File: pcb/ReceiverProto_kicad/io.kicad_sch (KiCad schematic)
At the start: 4 parts, among them J1 Conn_01x09, J2 Conn_01x03, J3 Conn_01x03, J4 Conn_01x06

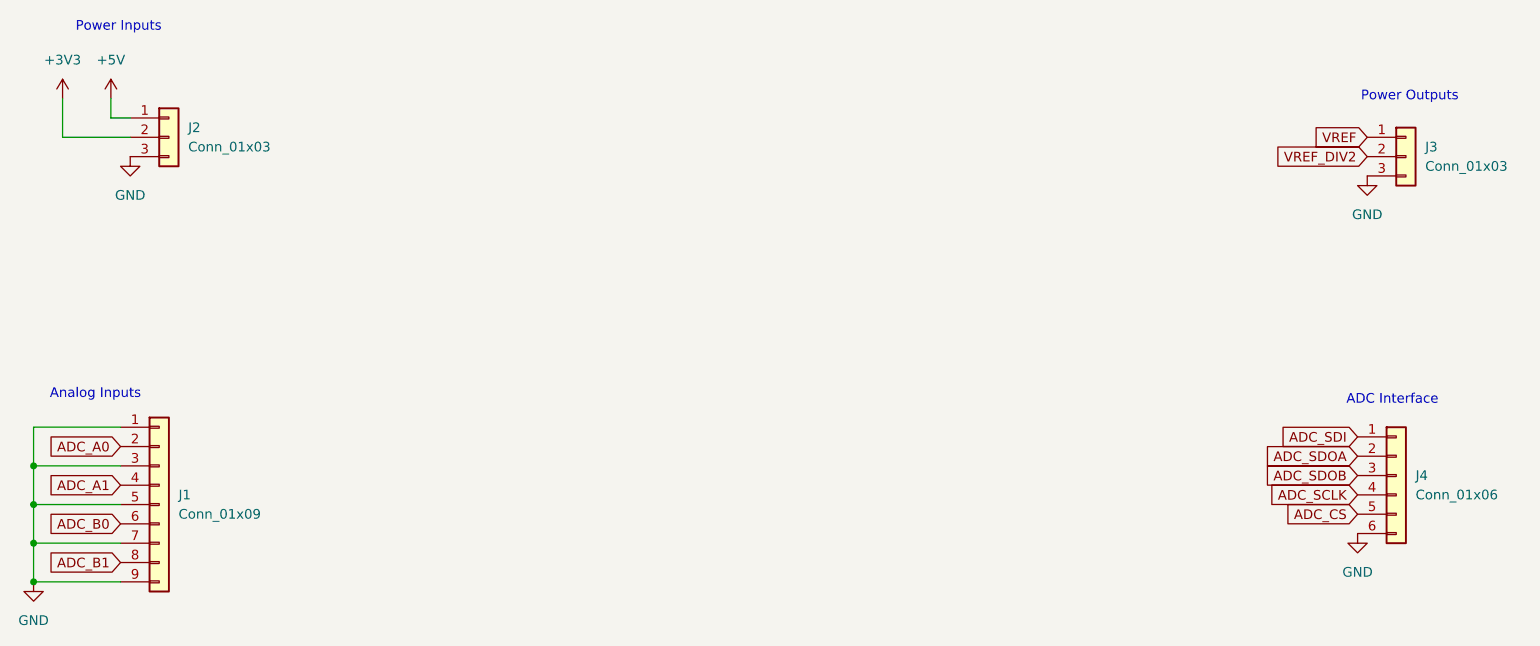
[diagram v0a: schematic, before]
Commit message: fixed kicad project, all footprints linked and no errors on board
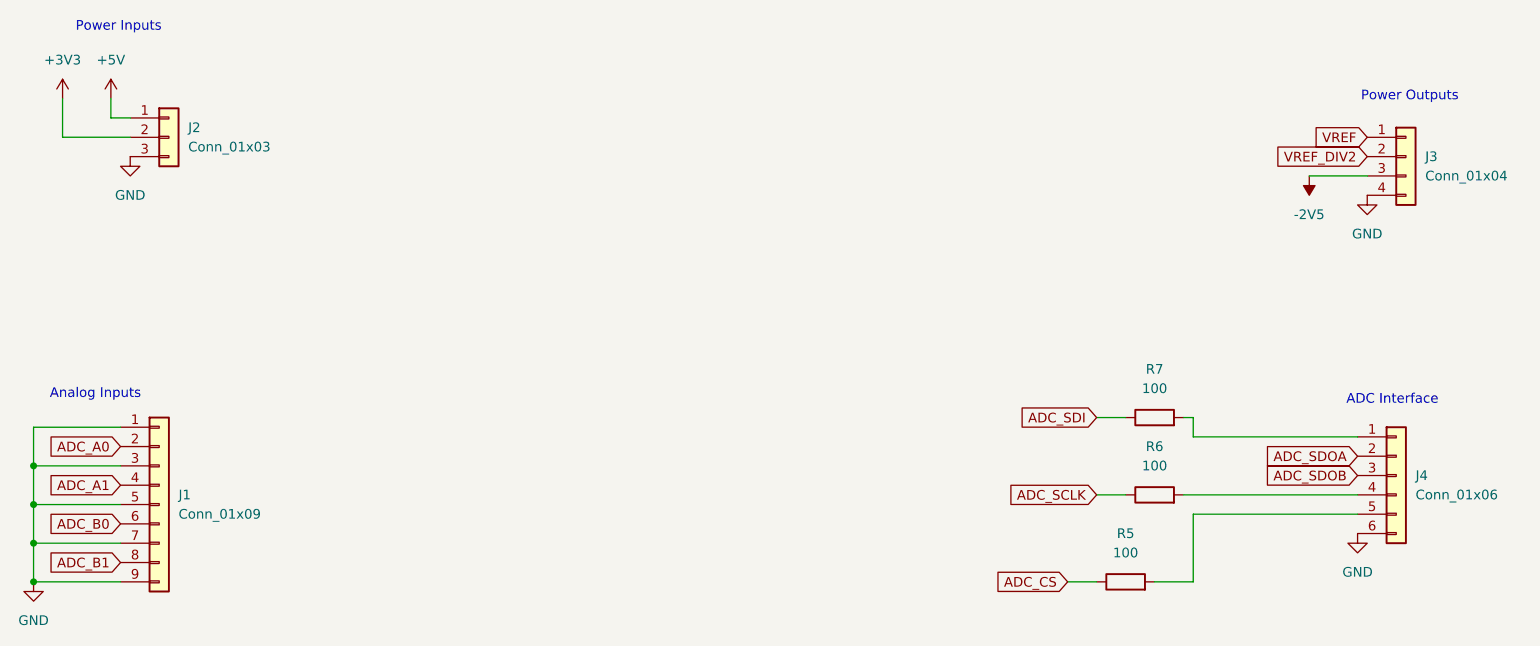
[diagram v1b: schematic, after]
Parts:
- removed J3: Conn_01x03, symbol Connector_Generic:Conn_01x03
- added J3: Conn_01x04, Connector_PinHeader_2.54mm:PinHeader_1x04_P2.54mm_Vertical, symbol Connector_Generic:Conn_01x04
- added R5, R6, R7: 100, SMD_Passives:YAG_R0201_YAG_100, symbol Device:R
- J1: footprint (none) -> Connector_PinHeader_2.54mm:PinHeader_1x09_P2.54mm_Vertical
- J2: footprint (none) -> Connector_PinHeader_2.54mm:PinHeader_1x03_P2.54mm_Vertical
- J4: footprint (none) -> Connector_PinHeader_2.54mm:PinHeader_1x06_P2.54mm_Vertical
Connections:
- net ADC_CS: now also R5.1; no longer J4.5 (Pin_5)
- net ADC_SCLK: now also R6.1; no longer J4.4 (Pin_4)
- net ADC_SDI: now also R7.1; no longer J4.1 (Pin_1)
- net GND: now also J3.4 (Pin_4)
- net VREF: now also J3.1 (Pin_1)
- net VREF_DIV2: now also J3.2 (Pin_2)
- new net: J4.5 (Pin_5), R5.2
- new net: J4.4 (Pin_4), R6.2
- new net: J4.1 (Pin_1), R7.2
- new net -2V5: J3.3 (Pin_3)
